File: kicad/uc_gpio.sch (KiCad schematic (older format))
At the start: 1 part, among them U1_? TMS320F28388DZWTS

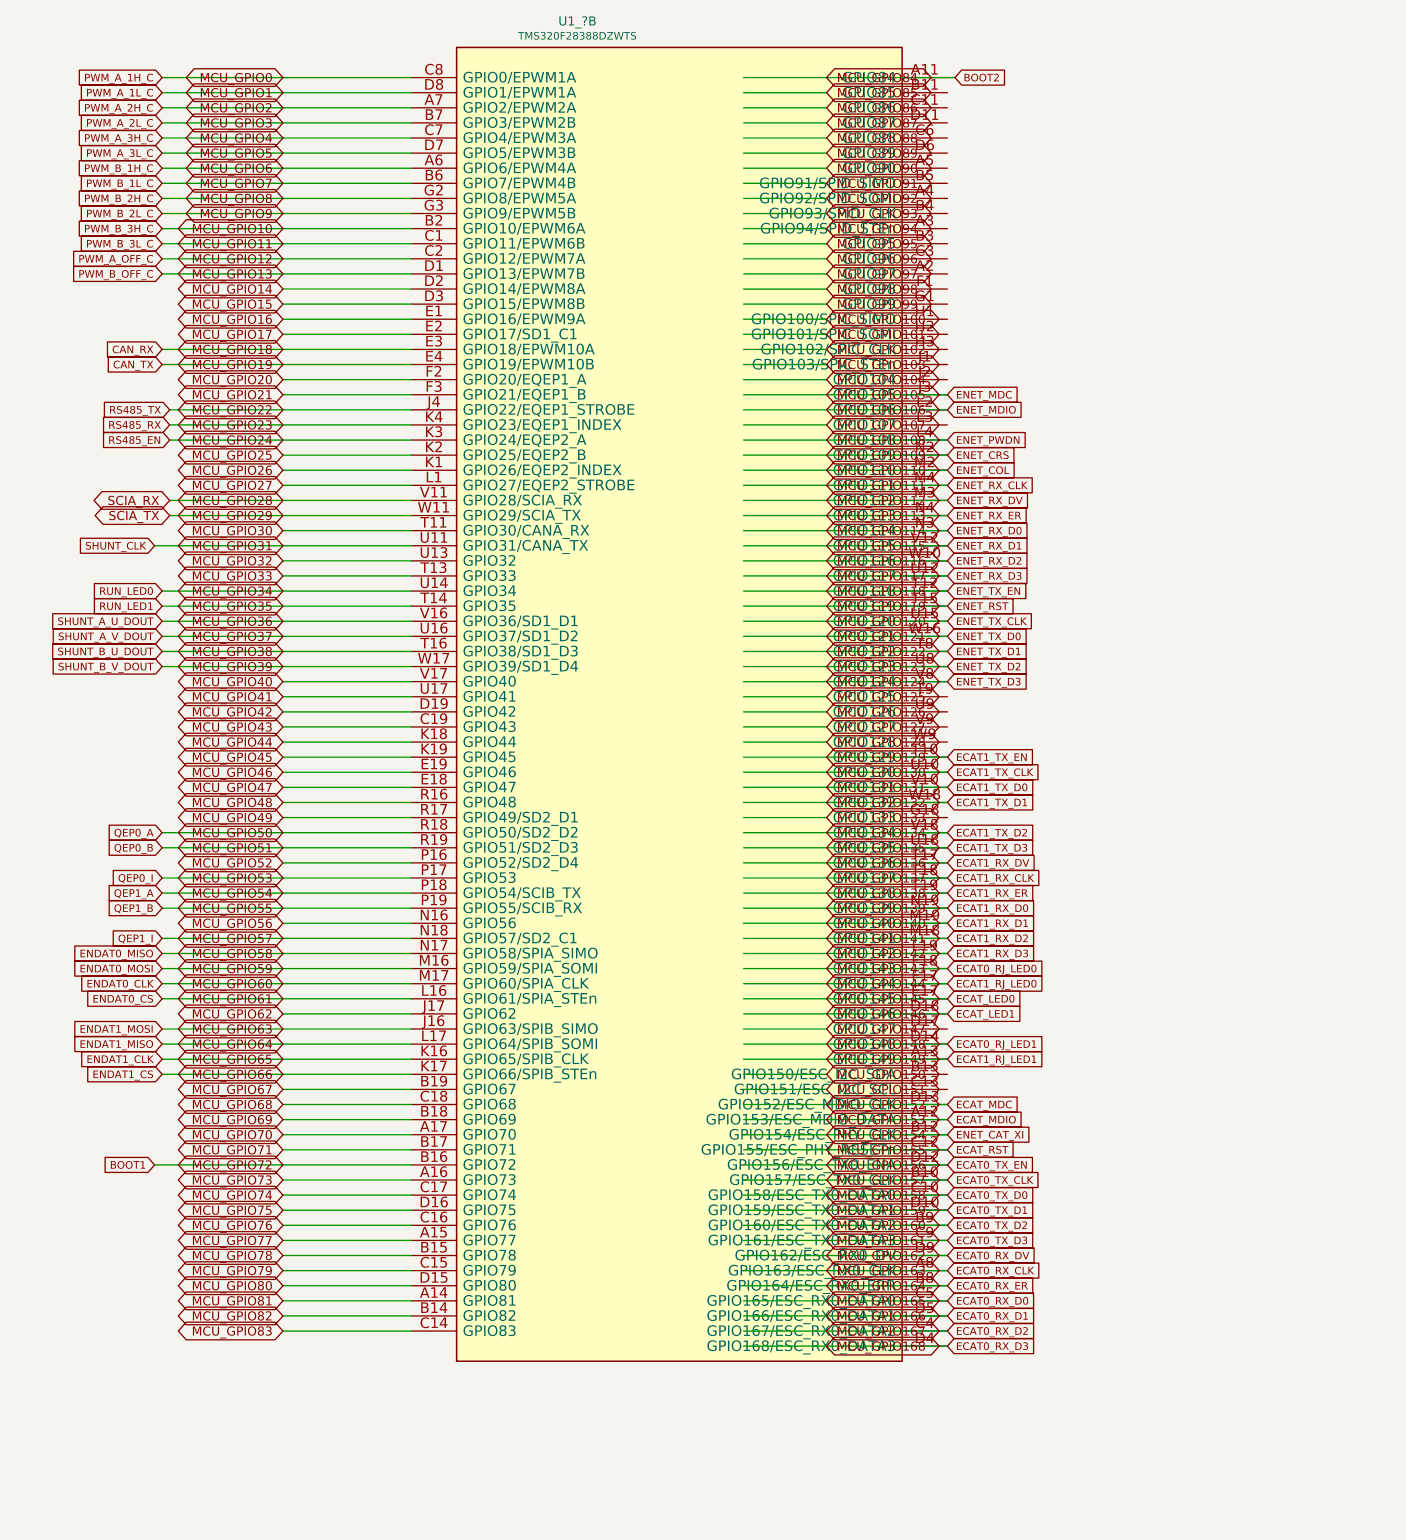
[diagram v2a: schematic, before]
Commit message: I've added LCD UI interfase, EQEP and finish ENDAT
I think I have almos all the interfases ready, I'm begining the
verigication process and then the part definig
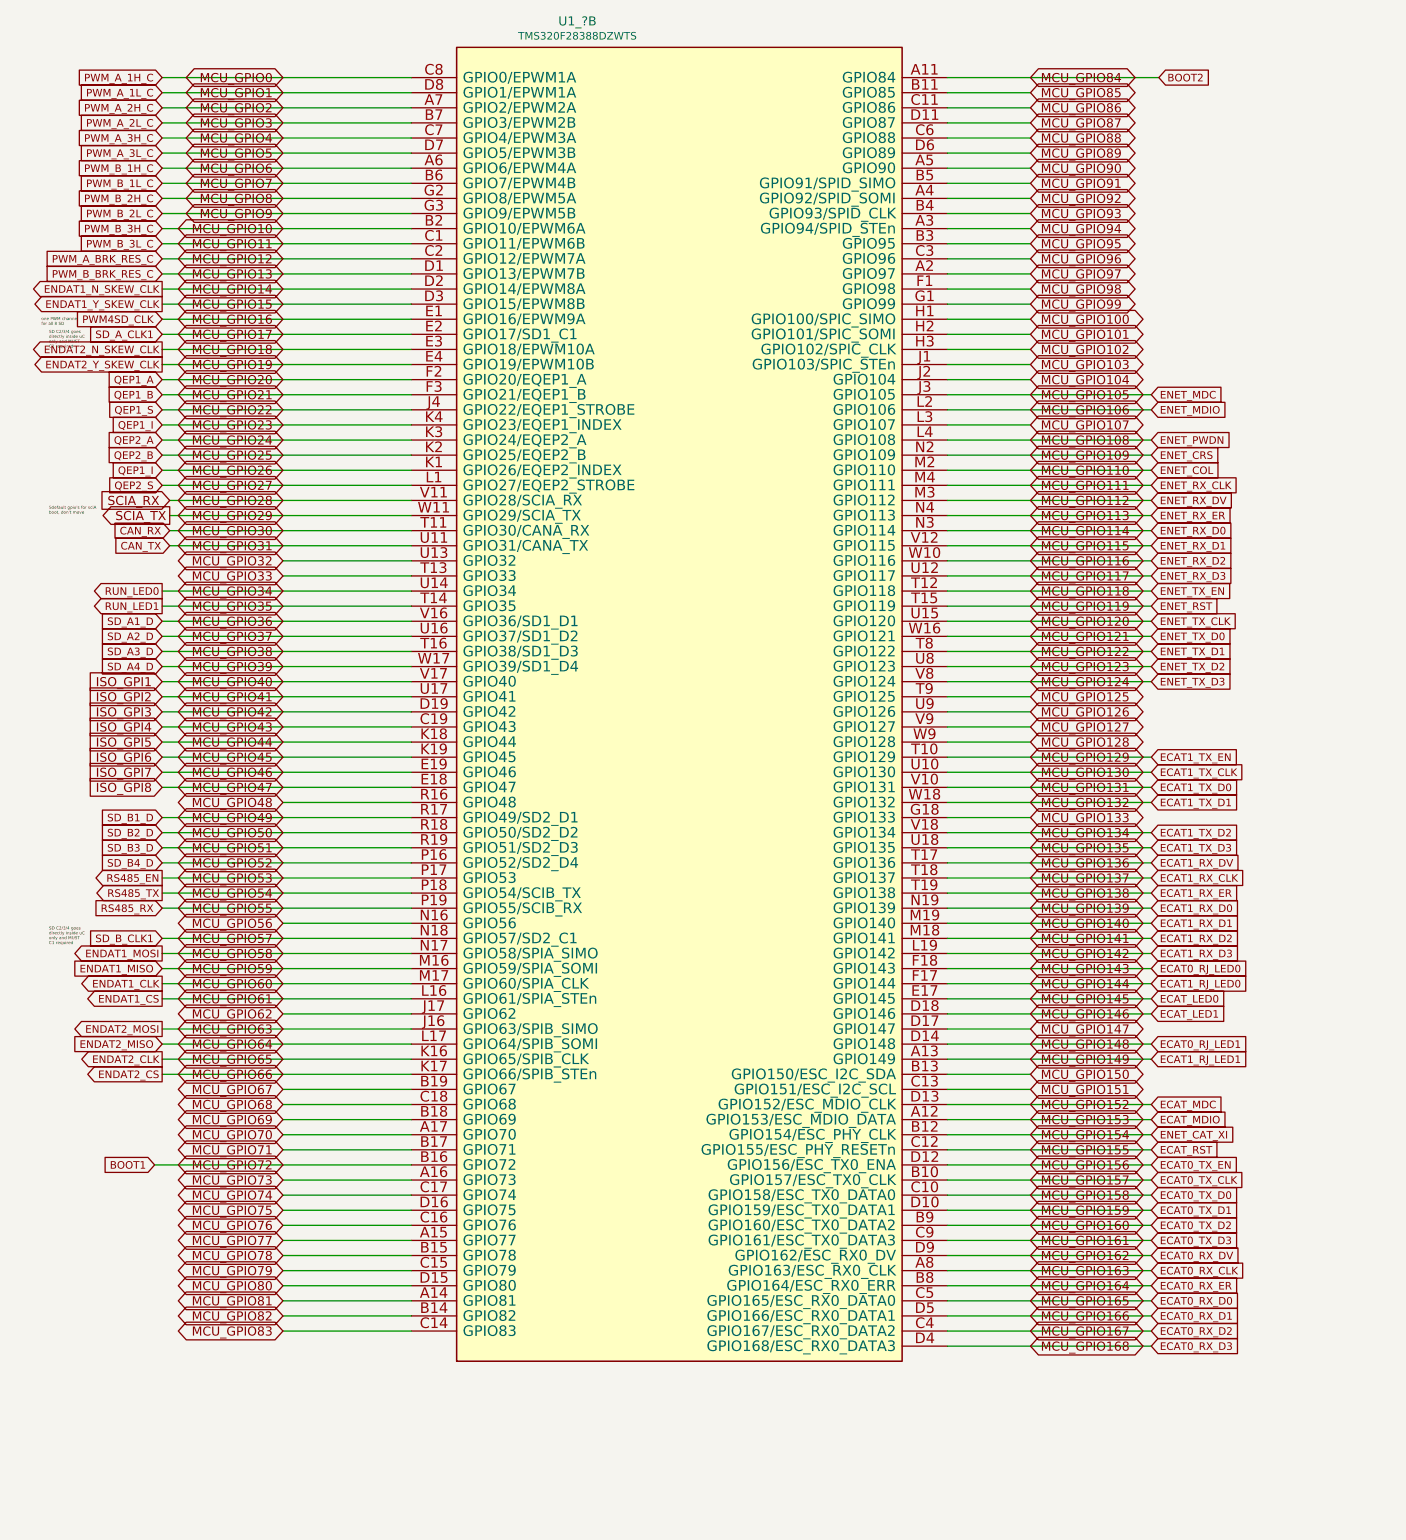
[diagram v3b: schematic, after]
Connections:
- net labels added: ENDAT1_N_SKEW_CLK, ENDAT1_Y_SKEW_CLK, ENDAT2_CLK, ENDAT2_CS, ENDAT2_MISO, ENDAT2_MOSI, ENDAT2_N_SKEW_CLK, ENDAT2_Y_SKEW_CLK, ISO_GPI1, ISO_GPI2, ISO_GPI3, ISO_GPI4, ISO_GPI5, ISO_GPI6, ISO_GPI7, ISO_GPI8, PWM4SD_CLK, PWM_A_BRK_RES_C, PWM_B_BRK_RES_C, QEP1_S, QEP2_A, QEP2_B, QEP2_S, SD_A1_D, SD_A2_D, SD_A3_D, SD_A4_D, SD_A_CLK1, SD_B1_D, SD_B2_D, SD_B3_D, SD_B4_D, SD_B_CLK1
- net labels removed: ENDAT0_CLK, ENDAT0_CS, ENDAT0_MISO, ENDAT0_MOSI, PWM_A_OFF_C, PWM_B_OFF_C, QEP0_A, QEP0_B, QEP0_I, SHUNT_A_U_DOUT, SHUNT_A_V_DOUT, SHUNT_B_U_DOUT, SHUNT_B_V_DOUT, SHUNT_CLK
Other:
- note added: "SD C2/3/4 goes \ndirectly inside uC\nonly and MUST \nC1 required"
- note added: "SD C2/3/4 goes\ndirectly inside uC\nonly and MUST \nC1 required"
- note added: "Sdefault gpio's for sciA \nboot, don't move"
- note added: "one PWM channel \nfor all 8 SD"

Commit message: improve ethercat, embedded rj45 to spare, remove some unnecesary r's
I've worked on ethetcat/net to improve visibility on A3 page and also
remove some R's related to leds and change the embedded Rj45 for the
spare transformer and connector 'cause half the price and more options
to choose the connector shape and position
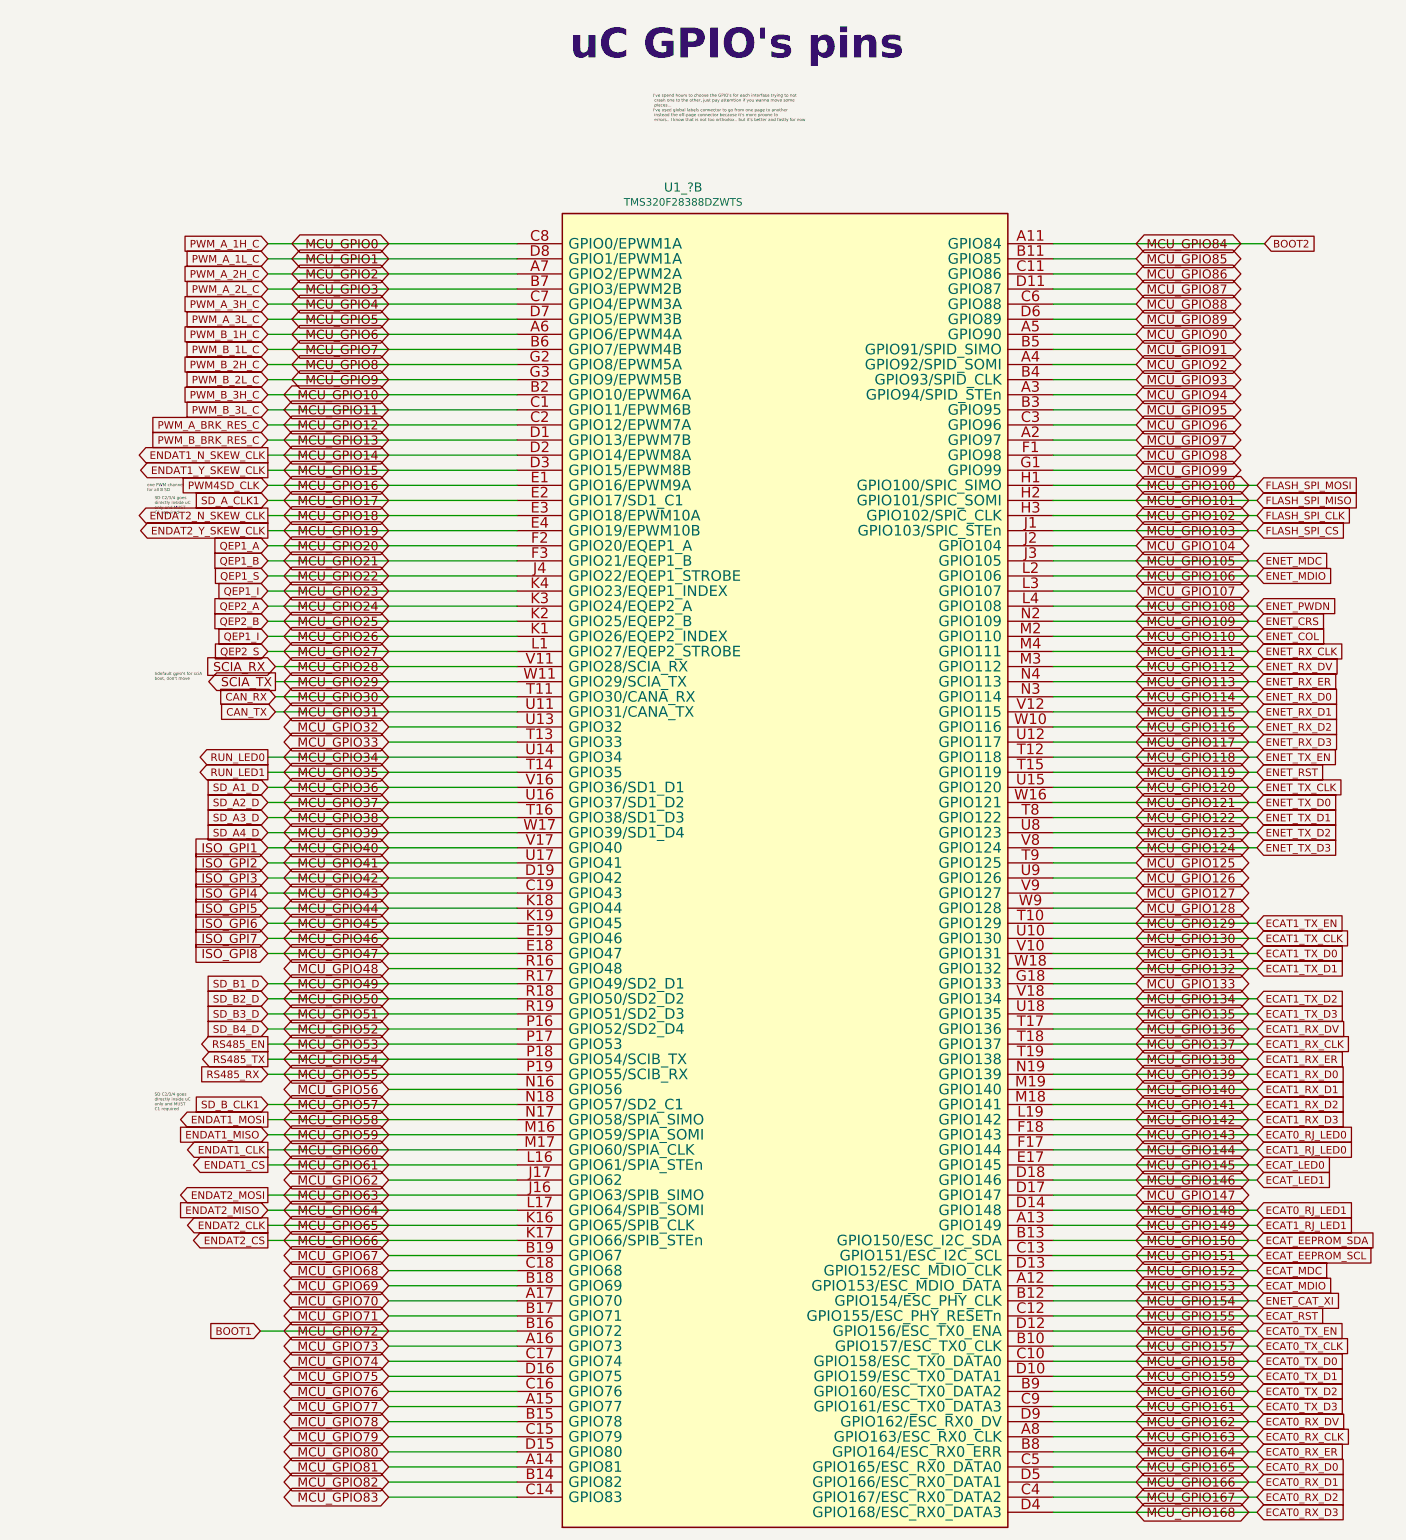
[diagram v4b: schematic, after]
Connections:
- net MCU_GPIO100 renamed FLASH_SPI_MOSI
- net MCU_GPIO101 renamed FLASH_SPI_MISO
- net MCU_GPIO102 renamed FLASH_SPI_CLK
- net MCU_GPIO103 renamed FLASH_SPI_CS
- net MCU_GPIO150 renamed ECAT_EEPROM_SDA
- net MCU_GPIO151 renamed ECAT_EEPROM_SCL
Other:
- note added: "I've spend hours to choose the GPIO's for each interfase trying to not\n crash one to the other, just pay attemtion if you wanna move some\n pieces...\nI've used global labels connector to go from one page to another\n instead the off-page connector because it's more proune to\n errors.. I know that is not too orthodox.. but it's better and fastly for now"
- note added: "uC GPIO's pins\n"
- moved on the sheet: U1_?B

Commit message: remove isolation GPIO's and replace it by free pins at IGBT
I remove completely the isolated inputs pins cause I've 8 pins free at
IGBT isolated interfase, so I leave 4 for outpus and 4 for inputs with
one isolated stage, the same as the previous isolated GPIO sheet..
I've improved the DBG sheet and some other details,. I'm ready to make
some electrical checks and fchoose the parts codes and footprints.. go
for it!
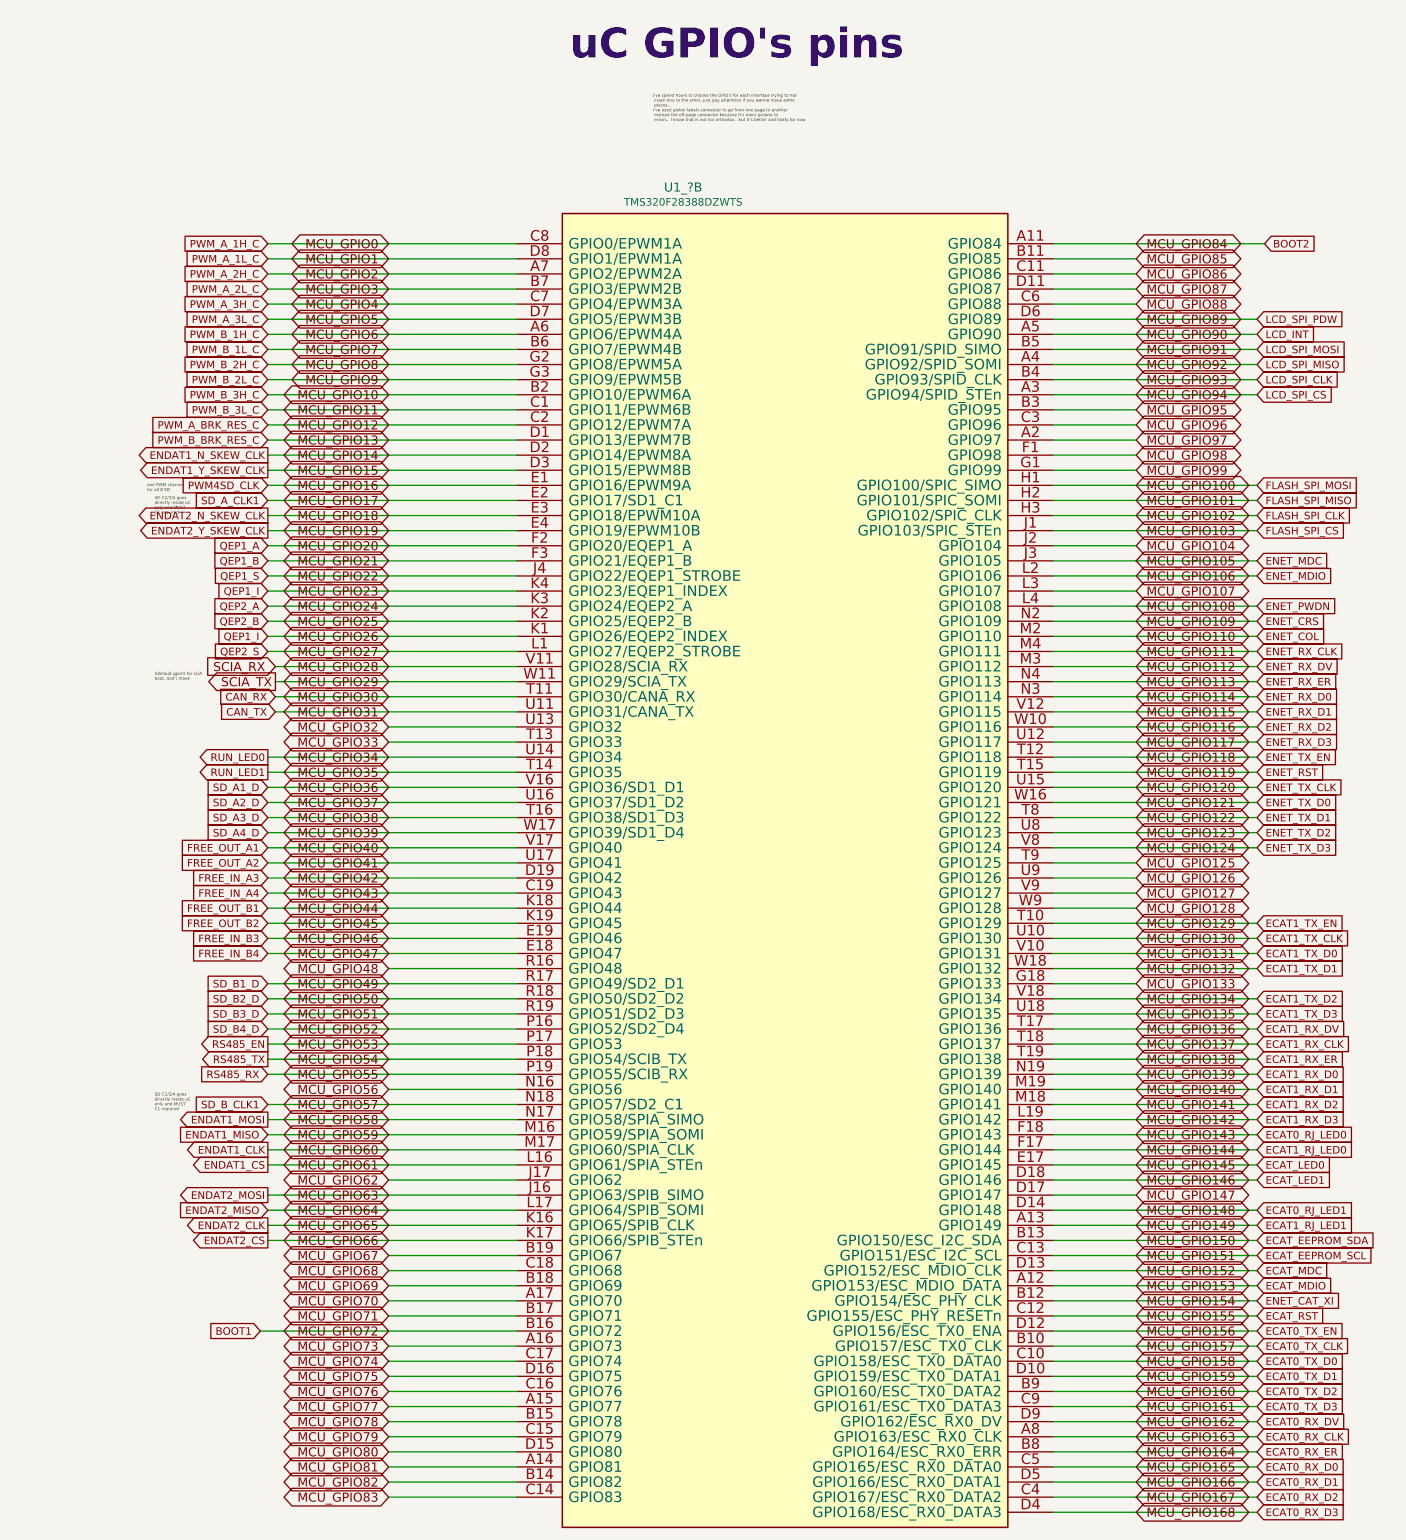
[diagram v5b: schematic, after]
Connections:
- net ISO_GPI1 renamed FREE_OUT_A1
- net ISO_GPI2 renamed FREE_OUT_A2
- net ISO_GPI3 renamed FREE_IN_A3
- net ISO_GPI4 renamed FREE_IN_A4
- net ISO_GPI5 renamed FREE_OUT_B1
- net ISO_GPI6 renamed FREE_OUT_B2
- net ISO_GPI7 renamed FREE_IN_B3
- net ISO_GPI8 renamed FREE_IN_B4
- net MCU_GPIO89 renamed LCD_SPI_PDW
- net MCU_GPIO90 renamed LCD_INT
- net MCU_GPIO91 renamed LCD_SPI_MOSI
- net MCU_GPIO92 renamed LCD_SPI_MISO
- net MCU_GPIO93 renamed LCD_SPI_CLK
- net MCU_GPIO94 renamed LCD_SPI_CS
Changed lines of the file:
@@
 $Descr A3 16535 11693
 encoding utf-8
-Sheet 14 19
+Sheet 14 18
 Title "gpio"
-Date "25 10 2019"
+Date "2020-01-09"
 Rev "1.0"
 Comp "dci"
@@
 	8350 3200 8900 3200
 Wire Wire Line
-	8350 3100 8900 3100
-Wire Wire Line
-	8350 3000 8900 3000
-Wire Wire Line
-	8350 2900 8900 2900
-Wire Wire Line
-	8350 2800 8900 2800
-Wire Wire Line
-	8350 2700 8900 2700
-Wire Wire Line
-	8350 2600 8900 2600
-Wire Wire Line
 	8350 2500 8900 2500
 Wire Wire Line
@@
 Wire Wire Line
 	3150 4800 4800 4800
-Text GLabel 3150 6100 0    60   Input ~ 0
-ISO_GPI1
-Text GLabel 3150 6200 0    60   Input ~ 0
-ISO_GPI2
-Text GLabel 3150 6300 0    60   Input ~ 0
-ISO_GPI3
-Text GLabel 3150 6400 0    60   Input ~ 0
-ISO_GPI4
-Text GLabel 3150 6500 0    60   Input ~ 0
-ISO_GPI5
-Text GLabel 3150 6600 0    60   Input ~ 0
-ISO_GPI6
-Text GLabel 3150 6700 0    60   Input ~ 0
-ISO_GPI7
-Text GLabel 3150 6800 0    60   Input ~ 0
-ISO_GPI8
 Wire Wire Line
 	3150 6100 4800 6100
@@
 Wire Wire Line
 	8350 8800 9700 8800
+Text GLabel 9700 3000 2    50   Input ~ 0
+LCD_SPI_CLK
+Text GLabel 9700 2800 2    50   Input ~ 0
+LCD_SPI_MOSI
+Text GLabel 9700 2700 2    50   Input ~ 0
+LCD_INT
+Text GLabel 9700 2900 2    50   Input ~ 0
+LCD_SPI_MISO
+Text GLabel 9700 3100 2    50   Input ~ 0
+LCD_SPI_CS
+Wire Wire Line
+	8350 2800 9700 2800
+Wire Wire Line
+	8350 2900 9700 2900
+Wire Wire Line
+	8350 3000 9700 3000
+Wire Wire Line
+	8350 3100 9700 3100
+Text GLabel 9700 2600 2    50   Input ~ 0
+LCD_SPI_PDW
+Wire Wire Line
+	8350 2700 9700 2700
+Wire Wire Line
+	8350 2600 9700 2600
+Text GLabel 3150 6100 0    50   Input ~ 0
+FREE_OUT_A1
+Text GLabel 3150 6200 0    50   Input ~ 0
+FREE_OUT_A2
+Text GLabel 3150 6300 0    50   Input ~ 0
+FREE_IN_A3
+Text GLabel 3150 6400 0    50   Input ~ 0
+FREE_IN_A4
+Text GLabel 3150 6500 0    50   Input ~ 0
+FREE_OUT_B1
+Text GLabel 3150 6600 0    50   Input ~ 0
+FREE_OUT_B2
+Text GLabel 3150 6700 0    50   Input ~ 0
+FREE_IN_B3
+Text GLabel 3150 6800 0    50   Input ~ 0
+FREE_IN_B4
 $EndSCHEMATC
